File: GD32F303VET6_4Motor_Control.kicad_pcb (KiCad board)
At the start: 6 copper layers, 100 x 60 mm, 119 parts, among them CN1 KF128L-5.08-2P, CN2 WJ15EDGRC-3.81-2P, CN4 WJ15EDGRC-3.81-2P, CN5 KF2EDGRM-3.81-6P, CN6 KF2EDGRM-3.81-6P, CN7 KF2EDGRM-3.81-6P, CN8 KF2EDGRM-3.81-6P, J1 TYPE-C-31-M-31, J2 TYPE-C 16PIN 2MD(073), Q3 CJ3134K KF, Q4 CJ3134K KF, SW1 SKRPACE010, U1 XL1509-5.0, U10 SIT3485ESA, U11 TXS0104EPWR, U13 CH340E, U14 TPD4S012DRYR, U2 B0503S-2WR3L, U3 SY8089A1AAC, U4 CH213K, U5 SY8089AAC, U6 GD32F303VET6, U7 ISO1050DWR, U9 π131U30, Y1 TAXM8M4RDBCCT2T, Y2 XKXGI-SUA-32.768K

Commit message: 更新六层电机控制板设计与器件库
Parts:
- removed U2: B0503S-2WR3L, Converter_DCDC:B0503S-2WR3L
- added U15: IB0505S-2W3L, kicad_api_lib:IB0505S-2W3L, F.Cu at (165.4, 94.0)
- C13, C15, C36: footprint Capacitor_SMD:C_0402_1005Metric_Pad0.74x0.62mm_HandSolder -> Capacitor_SMD:C_0603_1608Metric_Pad1.08x0.95mm_HandSolder
- C4: value 10uF -> 4.7uF
- L1: value 1uF -> MWTC201610S1R0MT; footprint Capacitor_SMD:C_0603_1608Metric_Pad1.08x0.95mm_HandSolder -> kicad_api_lib:MWTC201610S1R0MT
- R5: footprint Resistor_SMD:R_0402_1005Metric_Pad0.72x0.64mm_HandSolder -> Resistor_SMD:R_0603_1608Metric_Pad0.98x0.95mm_HandSolder
- R8, R9: footprint Resistor_SMD:R_01005_0402Metric_Pad0.57x0.30mm_HandSolder -> Resistor_SMD:R_0603_1608Metric_Pad0.98x0.95mm_HandSolder
- U7: footprint Package_SO:SOIC-16_3.9x9.9mm_P1.27mm -> Package_SO:SOIC-16W_7.5x10.3mm_P1.27mm
- moved R5 12.6 mm to (152.9, 96.8)
- moved R1 7.61 mm to (140.7, 108.2), turned to 180 degrees
- moved C15 7.42 mm to (146.7, 108.1), turned to 0 degrees
- moved D2 6.55 mm to (143.6, 107.3), turned to 90 degrees
- moved C14 5.74 mm to (146.7, 106.4), turned to 0 degrees
- moved C13 5.04 mm to (147.8, 97.6), turned to 90 degrees
- moved C10 4.87 mm to (151.0, 106.9), turned to 0 degrees
- moved C9 4.60 mm to (153.0, 104.4), turned to 180 degrees
- moved U5 3.80 mm to (151.5, 101.2)
- moved R8 3.22 mm to (149.4, 97.6), turned to 90 degrees
- moved R9 2.34 mm to (152.9, 98.4)
- moved L3 2.15 mm to (147.1, 103.1), turned to -90 degrees
- moved C5 1.65 mm to (160.4, 99.5)
- moved L1 1.35 mm to (160.8, 81.1), turned to -90 degrees
- moved U7 1.03 mm to (99.0, 101.5)
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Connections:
- C44 pad 2: +5V_ISO -> +3V3_ISO
- R1 pad 2: GNDS -> GND
- R27 pad 2: /MCU_Core/USB_TTL_CH340/CH_TX -> /MCU_Core/USB_TTL_CH340/CH_RX
- U13 pad 8: /MCU_Core/USB_TTL_CH340/CH_RX -> /MCU_Core/USB_TTL_CH340/CH_TX
- U13 pad 9: /MCU_Core/USB_TTL_CH340/CH_TX -> /MCU_Core/USB_TTL_CH340/CH_RX
- U6 pad 23: (no net) -> /MCU_Core/FG1_4
- U6 pad 96: /MCU_Core/FG1_4 -> (no net)
- U9 pad 12: /MCU_Core/RS485_TX -> /RS485/RS485_RX
- U9 pad 16: +5V_ISO -> +3V3_ISO
- U9 pad 3: /MCU_Core/RS485_RX -> /MCU_Core/RS485_TX
- U9 pad 5: /RS485/RS485_RX -> /MCU_Core/RS485_RX
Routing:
- net +5V_ISO: track 74.6 -> 17.4 mm, vias 3 -> 2
- net GND: track 206.1 -> 184.7 mm, vias 102 -> 148
- net /MCU_Core/FG1_4: track 40.6 -> 60.3 mm
- net GNDS: track 75.5 -> 63.8 mm, vias 33 -> 32
- net Net-(U5-EN): track 8.65 -> 19.2 mm
- net /MCU_Core/RS485_TX: track 56.3 -> 47.6 mm
- net +5V: track 94.2 -> 87.6 mm, vias 7 -> 31
- net Net-(U5-FB): track 5.14 -> 10.7 mm
- net +3V3_ISO: track 24.5 -> 29.8 mm, vias 2 -> 3
- net /MCU_Core/RS485_RX: track 47.8 -> 43.2 mm
- net /MCU_Core/DIR1_4: track 39.2 -> 43.2 mm
- net /MCU_Core/USB_TTL_CH340/CH_TX: track 21.6 -> 18.1 mm
- net /MCU_Core/CAN_RX: track 32.8 -> 36.1 mm
- net Net-(U3-LX): track 7.52 -> 5.11 mm
- net +3V3: track 121.6 -> 123.9 mm, vias 14 -> 26
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- added copper zone on F.Cu, net +3V3
- added copper zone on F.Cu, net +5V

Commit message: 更新电源与USB供电设计、PCB及器件库
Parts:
- removed the R27 at (108.0, 73.0)
- removed R35: 5.1K, Resistor_SMD:R_0402_1005Metric_Pad0.72x0.64mm_HandSolder
- removed U15: IB0505S-2W3L, kicad_api_lib:IB0505S-2W3L
- added C55: 1uF/10V, Capacitor_SMD:C_0603_1608Metric, B.Cu at (88.9, 74.5)
- added C56: 1uF/10V, Capacitor_SMD:C_0603_1608Metric, B.Cu at (88.8, 90.5)
- added C57: 4.7uF/10V, Capacitor_SMD:C_0603_1608Metric, F.Cu at (169.8, 93.3)
- added C58: 1uF/10V, Capacitor_SMD:C_0603_1608Metric, F.Cu at (173.5, 105.6)
- added R34: 5.1K, Resistor_SMD:R_0402_1005Metric_Pad0.72x0.64mm_HandSolder, F.Cu at (96.6, 91.8)
- added U16: LM66100DCKR, kicad_api_lib:LM66100DCKR, B.Cu at (90.8, 74.6)
- added U17: LM66100DCKR, kicad_api_lib:LM66100DCKR, B.Cu at (90.8, 90.4)
- added U18: LM66100DCKR, kicad_api_lib:LM66100DCKR, F.Cu at (173.2, 102.7)
- added U2: IB0505S-2W3L, kicad_api_lib:IB0505S-2W3L, F.Cu at (165.5, 94.0)
- C1: footprint Capacitor_SMD:CP_Elec_10x10.5 -> Capacitor_SMD:CP_Elec_8x10
- C5: footprint Capacitor_SMD:CP_Elec_5x5.4 -> Capacitor_SMD:CP_Elec_6.3x7.7
- C53: value 10uF -> 4.7uF
- moved D10 1.09 mm to (99.5, 86.3)
- moved D4 0.70 mm to (169.2, 99.7)
- moved R32 0.35 mm to (100.1, 89.1)
- moved L3 0.28 mm to (147.1, 102.8)
- moved D1 0.21 mm to (177.8, 108.7), turned to 180 degrees
- moved C13 0.20 mm to (147.6, 97.6)
- moved R8 0.20 mm to (149.2, 97.6)
- moved R31 0.15 mm to (100.1, 90.1)
- turned C16 to 0 degrees
- turned C21 to 180 degrees
- renumbered C4 to C3, C3 to C4, R28 to R27, R29 to R28, R30 to R29, R31 to R30, R32 to R31, R33 to R32, R34 to R33
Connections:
- C1 pad 1: Net-(D1-K) -> +24V
- C16 pad 2: Net-(C16-Pad2) -> /MCU_Core/OSCIN
- C21 pad 2: Net-(C21-Pad2) -> /MCU_Core/OSCOUT
- C5 pad 1: +5V -> BOARD_5V_RAW
- C53 pad 1: +5V -> USB1_VBUS
- C54 pad 1: +5V -> USB1_VBUS
- D1 pad 1: Net-(D1-K) -> +24V
- D1 pad 2: +24V -> GND
- J1 pad A4: +5V -> USB1_VBUS
- J1 pad A9: +5V -> USB1_VBUS
- J1 pad B4: +5V -> USB1_VBUS
- J1 pad B9: +5V -> USB1_VBUS
- J2 pad A4: +5V -> USB2_VBUS
- J2 pad A9: +5V -> USB2_VBUS
- J2 pad B4: +5V -> USB2_VBUS
- J2 pad B9: +5V -> USB2_VBUS
- L2 pad 2: +5V -> BOARD_5V_RAW
- U1 pad 1: Net-(D1-K) -> +24V
- U1 pad 3: +5V -> BOARD_5V_RAW
- U14 pad 6: +5V -> USB1_VBUS
- Y1 pad 2: Net-(C16-Pad2) -> GND
- Y1 pad 4: Net-(C21-Pad2) -> GND
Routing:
- net GND: track 184.7 -> 221.5 mm, vias 148 -> 155
- net Net-(D1-K): track 35.1 -> 0.00 mm
- net +24V: track 6.75 -> 38.2 mm
- net USB1_VBUS: track 0.00 -> 21.3 mm, vias 0 -> 2
- net USB2_VBUS: track 0.00 -> 11.2 mm, vias 0 -> 1
- net BOARD_5V_RAW: track 0.00 -> 7.25 mm, vias 0 -> 22
- net +5V: track 87.6 -> 93.2 mm, vias 31 -> 7
- net /MCU_Core/OSCOUT: track 12.4 -> 15.0 mm
- net Net-(C21-Pad2): track 2.16 -> 0.00 mm
- net /MCU_Core/USB_TTL_CH340/DP2: track 10.2 -> 12.3 mm
- net Net-(C16-Pad2): track 1.97 -> 0.00 mm
- net /MCU_Core/OSCIN: track 13.6 -> 15.5 mm
- net /MCU_Core/USB_TTL_CH340/DN2: track 11.7 -> 10.6 mm
- net /MCU_Core/USB_DP: track 21.8 -> 22.7 mm
- net Net-(U5-EN): track 19.2 -> 20.1 mm
- added copper zone on F.Cu, net BOARD_5V_RAW
- added copper zone on In2.Cu, net BOARD_5V_RAW
- removed copper zone on B.Cu, net GND

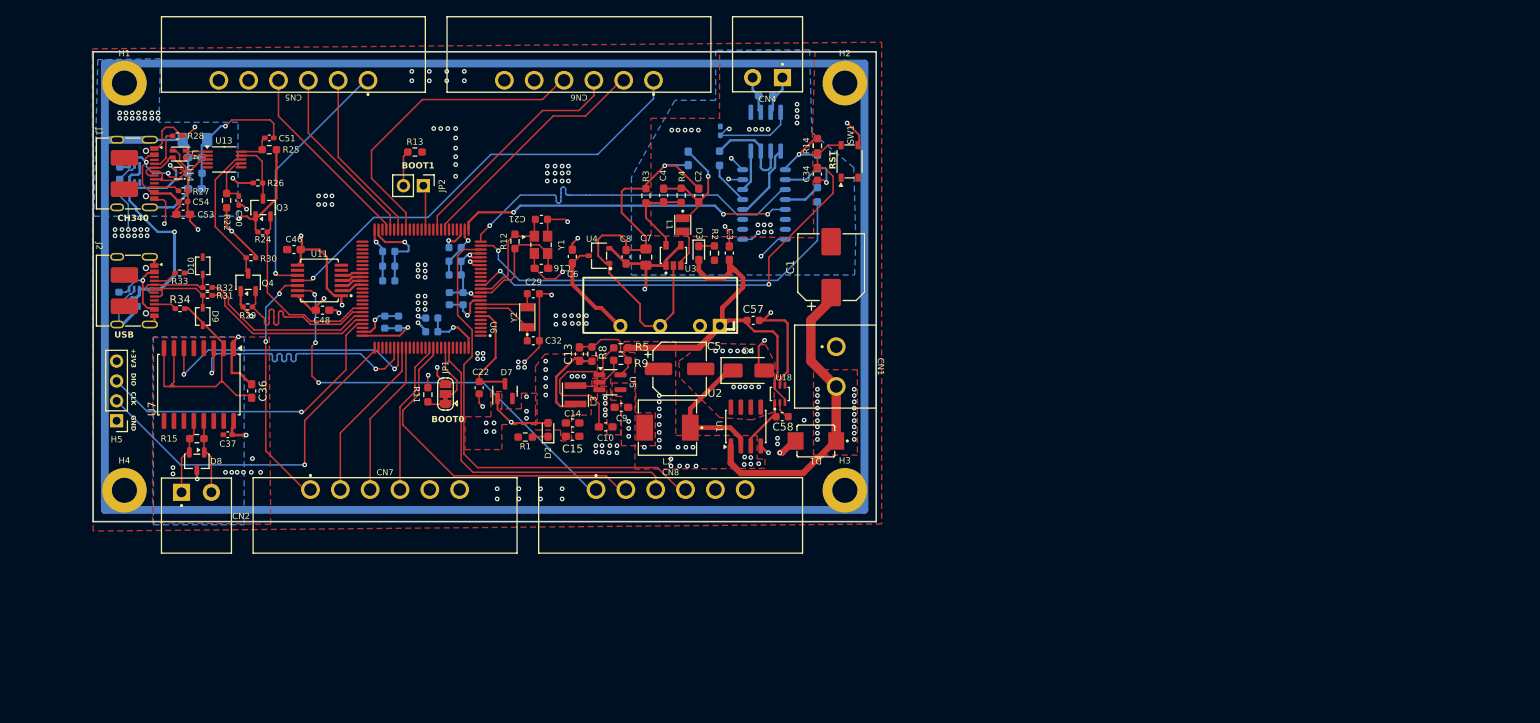
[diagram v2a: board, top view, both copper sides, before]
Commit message: V2.0: sync KiCad design, add firmware snapshot and README
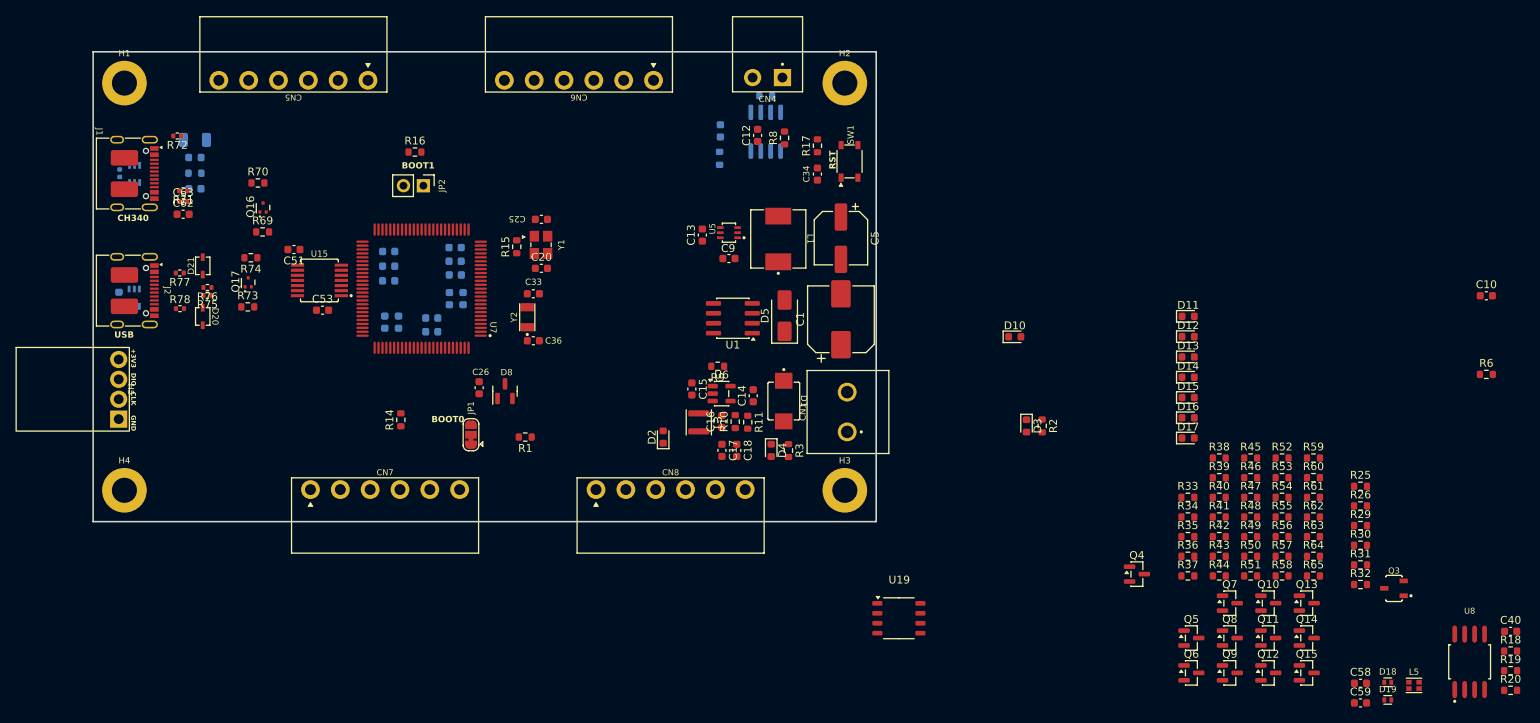
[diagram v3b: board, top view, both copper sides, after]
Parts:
- removed C2, C6: 10uF, Capacitor_SMD:C_0603_1608Metric_Pad1.08x0.95mm_HandSolder
- removed C3: 4.7uF, Capacitor_SMD:C_0603_1608Metric_Pad1.08x0.95mm_HandSolder
- removed the C36 at (105.8, 102.3)
- removed C37: 100nF, Capacitor_SMD:C_0402_1005Metric_Pad0.74x0.62mm_HandSolder
- removed C4: 22pF, Capacitor_SMD:C_0603_1608Metric_Pad1.08x0.95mm_HandSolder
- removed C43, C44: 0.1uF, Capacitor_SMD:C_0603_1608Metric_Pad1.08x0.95mm_HandSolder
- removed the C50 at (104.1, 78.0)
- removed the C51 at (108.0, 70.0)
- removed C7: 10uF, Capacitor_SMD:C_0805_2012Metric_Pad1.18x1.45mm_HandSolder
- removed C8: 1uF, Capacitor_SMD:C_0603_1608Metric_Pad1.08x0.95mm_HandSolder
- removed CN2: WJ15EDGRC-3.81-2P, kicad_api_lib:WJ15EDGRC-3.81-2P
- removed the D8 at (98.8, 111.3)
- removed the L1 at (160.8, 81.1)
- removed L4: PCAQ2012B-900T040, Inductor_SMD:L_CommonModeChoke_Coilcraft_0805USB
- removed the R15 at (98.8, 108.4)
- removed R22: 0, Resistor_SMD:R_0603_1608Metric_Pad0.98x0.95mm_HandSolder
- removed R4: 100k, Resistor_SMD:R_0603_1608Metric_Pad0.98x0.95mm_HandSolder
- removed the U13 at (102.2, 72.8)
- removed U14: TPD4S012DRYR, Package_DFN_QFN:TPD4S012DRYR
- removed U2: IB0505S-2W3L, kicad_api_lib:IB0505S-2W3L
- removed U3: SY8089A1AAC, kicad_api_lib:SY8089A1AAC
- removed U4: CH213K, kicad_api_lib:CH213K
- removed the U7 at (99.0, 101.5)
- removed U9: π131U30, kicad_api_lib:π131U30
- added C10: 1nF, Capacitor_SMD:C_0603_1608Metric, F.Cu at (263.4, 90.2)
- added C12: 1nF, Capacitor_SMD:C_0603_1608Metric, F.Cu at (170.4, 69.7)
- added C40: 100nF, Capacitor_SMD:C_0603_1608Metric, F.Cu at (266.5, 133.0)
- added C58: 1uF, Capacitor_SMD:C_0603_1608Metric, F.Cu at (247.4, 139.6)
- added C59: 100nF, Capacitor_SMD:C_0603_1608Metric, F.Cu at (247.4, 142.2)
- added D10: DIR_CMD_GREEN, LED_SMD:LED_0603_1608Metric, F.Cu at (203.2, 95.4)
- added D11: RELEASE_YELLOW, LED_SMD:LED_0603_1608Metric, F.Cu at (225.3, 92.8)
- added D12: DIR_CMD_GREEN, LED_SMD:LED_0603_1608Metric, F.Cu at (225.3, 95.4)
- added D13: RELEASE_YELLOW, LED_SMD:LED_0603_1608Metric, F.Cu at (225.3, 98.0)
- added D14: DIR_CMD_GREEN, LED_SMD:LED_0603_1608Metric, F.Cu at (225.3, 100.6)
- added D15: RELEASE_YELLOW, LED_SMD:LED_0603_1608Metric, F.Cu at (225.3, 103.1)
- added D16: DIR_CMD_GREEN, LED_SMD:LED_0603_1608Metric, F.Cu at (225.3, 105.7)
- added D17: RELEASE_YELLOW, LED_SMD:LED_0603_1608Metric, F.Cu at (225.3, 108.3)
- added D18: KLXES15AAA1, kicad_api_lib:KLXES15AAA1, F.Cu at (250.8, 139.5)
- added D19: KLXES15AAA1, kicad_api_lib:KLXES15AAA1, F.Cu at (250.8, 141.8)
- added D4: LED, LED_SMD:LED_0603_1608Metric, F.Cu at (172.1, 109.9)
- added L5: PCAQ2012B-900T040, kicad_api_lib:PCAQ2012B-900T040, F.Cu at (254.2, 139.9)
- added Q10: CJ3134K, Package_TO_SOT_SMD:SOT-23, F.Cu at (235.6, 129.4)
- added Q11: CJ3134K, Package_TO_SOT_SMD:SOT-23, F.Cu at (235.6, 133.9)
- added Q12: CJ3134K, Package_TO_SOT_SMD:SOT-23, F.Cu at (235.6, 138.3)
- added Q13: CJ3134K, Package_TO_SOT_SMD:SOT-23, F.Cu at (240.5, 129.4)
- added Q14: CJ3134K, Package_TO_SOT_SMD:SOT-23, F.Cu at (240.5, 133.9)
- added Q15: CJ3134K, Package_TO_SOT_SMD:SOT-23, F.Cu at (240.5, 138.3)
- added Q3: CJ3134K, kicad_api_lib:CJ3134K, F.Cu at (251.6, 127.5)
- added Q4: CJ3134K, Package_TO_SOT_SMD:SOT-23, F.Cu at (218.8, 125.7)
- added Q5: CJ3134K, Package_TO_SOT_SMD:SOT-23, F.Cu at (225.8, 133.9)
- added Q6: CJ3134K, Package_TO_SOT_SMD:SOT-23, F.Cu at (225.8, 138.3)
- added Q7: CJ3134K, Package_TO_SOT_SMD:SOT-23, F.Cu at (230.7, 129.4)
- added Q8: CJ3134K, Package_TO_SOT_SMD:SOT-23, F.Cu at (230.7, 133.9)
- added Q9: CJ3134K, Package_TO_SOT_SMD:SOT-23, F.Cu at (230.7, 138.3)
- added R19: 10kΩ, Resistor_SMD:R_0603_1608Metric, F.Cu at (266.5, 138.0)
- added R20: 10kΩ, Resistor_SMD:R_0603_1608Metric, F.Cu at (266.5, 140.5)
- added R26: 360, Resistor_SMD:R_0603_1608Metric, F.Cu at (247.4, 117.0)
- added R29: AF0603JR-0710KL, Resistor_SMD:R_0603_1608Metric, F.Cu at (247.4, 119.5)
- added R30: AF0603JR-0710KL, Resistor_SMD:R_0603_1608Metric, F.Cu at (247.4, 122.0)
- added R31: 330, Resistor_SMD:R_0603_1608Metric, F.Cu at (247.4, 124.5)
- added R32: 4.7k, Resistor_SMD:R_0603_1608Metric, F.Cu at (247.4, 127.0)
- added R33: 100, Resistor_SMD:R_0603_1608Metric, F.Cu at (225.3, 115.9)
- added R34: 1k, Resistor_SMD:R_0603_1608Metric, F.Cu at (225.3, 118.4)
- added R35: 1k, Resistor_SMD:R_0603_1608Metric, F.Cu at (225.3, 120.9)
- added R36: 100, Resistor_SMD:R_0603_1608Metric, F.Cu at (225.3, 123.4)
- added R37: 1k, Resistor_SMD:R_0603_1608Metric, F.Cu at (225.3, 125.9)
- added R38: 1k, Resistor_SMD:R_0603_1608Metric, F.Cu at (229.3, 110.9)
- added R39: 10k, Resistor_SMD:R_0603_1608Metric, F.Cu at (229.3, 113.4)
- added R40: 10k, Resistor_SMD:R_0603_1608Metric, F.Cu at (229.3, 115.9)
- added R41: 10kΩ, Resistor_SMD:R_0603_1608Metric, F.Cu at (229.3, 118.4)
- added R42: 100, Resistor_SMD:R_0603_1608Metric, F.Cu at (229.3, 120.9)
- added R43: 100, Resistor_SMD:R_0603_1608Metric, F.Cu at (229.3, 123.4)
- added R44: 10k, Resistor_SMD:R_0603_1608Metric, F.Cu at (229.3, 125.9)
- added R45: 10k, Resistor_SMD:R_0603_1608Metric, F.Cu at (233.3, 110.9)
- added R46: 4.7kΩ, Resistor_SMD:R_0603_1608Metric, F.Cu at (233.3, 113.4)
- added R47: 4.7kΩ, Resistor_SMD:R_0603_1608Metric, F.Cu at (233.3, 115.9)
- added R48: 10k, Resistor_SMD:R_0603_1608Metric, F.Cu at (233.3, 118.4)
- added R49: 10k, Resistor_SMD:R_0603_1608Metric, F.Cu at (233.3, 120.9)
- added R50: 4.7kΩ, Resistor_SMD:R_0603_1608Metric, F.Cu at (233.3, 123.4)
- added R51: 4.7kΩ, Resistor_SMD:R_0603_1608Metric, F.Cu at (233.3, 125.9)
- added R52: 100, Resistor_SMD:R_0603_1608Metric, F.Cu at (237.3, 110.9)
- added R53: 1k, Resistor_SMD:R_0603_1608Metric, F.Cu at (237.3, 113.4)
- added R54: 1k, Resistor_SMD:R_0603_1608Metric, F.Cu at (237.3, 115.9)
- added R55: 100, Resistor_SMD:R_0603_1608Metric, F.Cu at (237.3, 118.4)
- added R56: 1k, Resistor_SMD:R_0603_1608Metric, F.Cu at (237.3, 120.9)
- added R57: 1k, Resistor_SMD:R_0603_1608Metric, F.Cu at (237.3, 123.4)
- added R58: 10k, Resistor_SMD:R_0603_1608Metric, F.Cu at (237.3, 125.9)
- added R59: 10k, Resistor_SMD:R_0603_1608Metric, F.Cu at (241.3, 110.9)
- added R6: 1MΩ, Resistor_SMD:R_0603_1608Metric, F.Cu at (263.4, 100.2)
- added R60: 100, Resistor_SMD:R_0603_1608Metric, F.Cu at (241.3, 113.4)
- added R61: 100, Resistor_SMD:R_0603_1608Metric, F.Cu at (241.3, 115.9)
- added R62: 10k, Resistor_SMD:R_0603_1608Metric, F.Cu at (241.3, 118.4)
- added R63: 10k, Resistor_SMD:R_0603_1608Metric, F.Cu at (241.3, 120.9)
- added R64: 10k, Resistor_SMD:R_0603_1608Metric, F.Cu at (241.3, 123.4)
- added R65: 10k, Resistor_SMD:R_0603_1608Metric, F.Cu at (241.3, 125.9)
- added R8: 1MΩ, Resistor_SMD:R_0603_1608Metric, F.Cu at (173.8, 70.0)
- added U19: CH340N, kicad_api_lib:CH340N, F.Cu at (188.4, 131.3)
- added U8: GD25Q16ESIGR, kicad_api_lib:GD25Q16ESIGR, F.Cu at (261.3, 136.9)
- C1: value 470µF -> RVT1E471M0810; footprint Capacitor_SMD:CP_Elec_8x10 -> kicad_api_lib:RVT1E471M0810
- C11: footprint Capacitor_SMD:C_0603_1608Metric_Pad1.08x0.95mm_HandSolder -> Capacitor_SMD:C_0603_1608Metric
- C13: renamed from C57; value 4.7uF/10V -> 1uF/10V
- C14: renamed from C9; value 10uF -> 22uF; footprint Capacitor_SMD:C_0603_1608Metric_Pad1.08x0.95mm_HandSolder -> Capacitor_SMD:C_0603_1608Metric
- C15: renamed from C10; footprint Capacitor_SMD:C_0603_1608Metric_Pad1.08x0.95mm_HandSolder -> Capacitor_SMD:C_0603_1608Metric
- C16: renamed from C13; value 100nF -> 22pF; footprint Capacitor_SMD:C_0603_1608Metric_Pad1.08x0.95mm_HandSolder -> Capacitor_SMD:C_0603_1608Metric
- C17: renamed from C14; footprint Capacitor_SMD:C_0603_1608Metric_Pad1.08x0.95mm_HandSolder -> Capacitor_SMD:C_0603_1608Metric
- C18: renamed from C15; footprint Capacitor_SMD:C_0603_1608Metric_Pad1.08x0.95mm_HandSolder -> Capacitor_SMD:C_0603_1608Metric
- C20: renamed from C16; value 22pF -> 15pF; footprint Capacitor_SMD:C_0603_1608Metric_Pad1.08x0.95mm_HandSolder -> Capacitor_SMD:C_0603_1608Metric
- C25: renamed from C21; value 22pF -> 15pF
- C33: renamed from C29; value 12pF -> 15pF
- C36: renamed from C32; value 12pF -> 15pF
- C5: value 220µF -> RVT1E221M0607; footprint Capacitor_SMD:CP_Elec_6.3x7.7 -> kicad_api_lib:RVT1E221M0607
- C50: renamed from C45; footprint Capacitor_SMD:C_0402_1005Metric_Pad0.74x0.62mm_HandSolder -> Capacitor_SMD:C_0603_1608Metric
- C51: renamed from C46; value 0.1uF -> 100nF; footprint Capacitor_SMD:C_0603_1608Metric_Pad1.08x0.95mm_HandSolder -> Capacitor_SMD:C_0603_1608Metric
- C53: renamed from C48; value 0.1uF -> 100nF; footprint Capacitor_SMD:C_0603_1608Metric_Pad1.08x0.95mm_HandSolder -> Capacitor_SMD:C_0603_1608Metric
- C57: renamed from C55; footprint Capacitor_SMD:C_0603_1608Metric -> Capacitor_SMD:C_0402_1005Metric
- C60: renamed from C52; value 1nF -> CC1206MKX7RDBB102; footprint Capacitor_SMD:C_1206_3216Metric_Pad1.33x1.80mm_HandSolder -> kicad_api_lib:CC1206MKX7RDBB102
- C62: renamed from C53; value 4.7uF -> 0603X106M100NT; footprint Capacitor_SMD:C_0603_1608Metric_Pad1.08x0.95mm_HandSolder -> Capacitor_SMD:C_0603_1608Metric
- C63: renamed from C54; value 100nF -> C1005X5R1H104K050BB; footprint Capacitor_SMD:C_0402_1005Metric_Pad0.74x0.62mm_HandSolder -> Capacitor_SMD:C_0402_1005Metric
- CN5, CN6, CN7, CN8: value KF2EDGRM-3.81-6P -> KF15EDGRC3.81-6P; footprint kicad_api_lib:KF2EDGRM-3.81-6P -> kicad_api_lib:KF15EDGRC3.81-6P
- D2, D3: footprint LED_SMD:LED_0603_1608Metric_Pad1.05x0.95mm_HandSolder -> LED_SMD:LED_0603_1608Metric
- FB2: value 100ohm@100MHz -> UPZ1608E101-3R0TF; footprint Capacitor_SMD:C_0603_1608Metric_Pad1.08x0.95mm_HandSolder -> kicad_api_lib:UPZ1608E101-3R0TF
- H5: footprint Connector_PinHeader_2.54mm:PinHeader_1x04_P2.54mm_Vertical -> kicad_api_lib:X9254WR-04-N0SN
- J1, J2: footprint kicad_api_lib:TYPE-C 16PIN 2MD NEW(073) -> kicad_api_lib:TYPE-C-31-M-31
- L3: footprint Inductor_SMD_Wurth:L_Wurth_WE-LQSH-3012 -> kicad_api_lib:SWPA3015S2R2NT
- Q16: renamed from Q3; footprint Package_TO_SOT_SMD:SOT-23-3 -> kicad_api_lib:CJ3134K KF
- Q17: renamed from Q4; footprint Package_TO_SOT_SMD:SOT-23-3 -> kicad_api_lib:CJ3134K KF
- R1, R2: value 10k -> 10kΩ; footprint Resistor_SMD:R_0603_1608Metric_Pad0.98x0.95mm_HandSolder -> Resistor_SMD:R_0603_1608Metric
- R10: renamed from R8; value 100K -> 100k; footprint Resistor_SMD:R_0603_1608Metric_Pad0.98x0.95mm_HandSolder -> Resistor_SMD:R_0603_1608Metric
- R11: renamed from R9; value 22K -> 22.1k; footprint Resistor_SMD:R_0603_1608Metric_Pad0.98x0.95mm_HandSolder -> Resistor_SMD:R_0603_1608Metric
- R14: renamed from R11; footprint Resistor_SMD:R_0603_1608Metric_Pad0.98x0.95mm_HandSolder -> Resistor_SMD:R_0603_1608Metric
- R15: renamed from R12; footprint Resistor_SMD:R_0603_1608Metric_Pad0.98x0.95mm_HandSolder -> Resistor_SMD:R_0603_1608Metric
- R16: renamed from R13; footprint Resistor_SMD:R_0603_1608Metric_Pad0.98x0.95mm_HandSolder -> Resistor_SMD:R_0603_1608Metric
- R17: renamed from R14; footprint Resistor_SMD:R_0603_1608Metric_Pad0.98x0.95mm_HandSolder -> Resistor_SMD:R_0603_1608Metric
- R18: value 10K -> 10kΩ; footprint Resistor_SMD:R_0603_1608Metric_Pad0.98x0.95mm_HandSolder -> Resistor_SMD:R_0603_1608Metric; moved to F.Cu
- R25: value 0 -> 360; footprint Resistor_SMD:R_0603_1608Metric_Pad0.98x0.95mm_HandSolder -> Resistor_SMD:R_0603_1608Metric
- R27: renamed from R19; value 120 -> CRCW0603120RFKEA; footprint Resistor_SMD:R_0603_1608Metric_Pad0.98x0.95mm_HandSolder -> Resistor_SMD:R_0603_1608Metric
- R28: renamed from R20; value 10K -> 1k; footprint Resistor_SMD:R_0603_1608Metric_Pad0.98x0.95mm_HandSolder -> Resistor_SMD:R_0603_1608Metric
- R3: value 22.1k -> 10kΩ; footprint Resistor_SMD:R_0603_1608Metric_Pad0.98x0.95mm_HandSolder -> Resistor_SMD:R_0603_1608Metric
- R69: renamed from R24; value 4.7K -> 4.7k; footprint Resistor_SMD:R_0402_1005Metric_Pad0.72x0.64mm_HandSolder -> Resistor_SMD:R_0603_1608Metric
- R7: renamed from R6; value 1M -> 1MΩ; footprint Resistor_SMD:R_0603_1608Metric_Pad0.98x0.95mm_HandSolder -> Resistor_SMD:R_0603_1608Metric
- R70: renamed from R26; value 4.7K -> 4.7k; footprint Resistor_SMD:R_0402_1005Metric_Pad0.72x0.64mm_HandSolder -> Resistor_SMD:R_0603_1608Metric
- R71: renamed from R27; value 5.1K -> RC0402FR-075K1L; footprint Resistor_SMD:R_0402_1005Metric_Pad0.72x0.64mm_HandSolder -> Resistor_SMD:R_0402_1005Metric
- R72: renamed from R28; value 5.1K -> RC0402FR-075K1L; footprint Resistor_SMD:R_0402_1005Metric_Pad0.72x0.64mm_HandSolder -> Resistor_SMD:R_0402_1005Metric
- R73: renamed from R29; value 4.7K -> 4.7k; footprint Resistor_SMD:R_0402_1005Metric_Pad0.72x0.64mm_HandSolder -> Resistor_SMD:R_0603_1608Metric
- R74: renamed from R30; value 4.7K -> 4.7k; footprint Resistor_SMD:R_0402_1005Metric_Pad0.72x0.64mm_HandSolder -> Resistor_SMD:R_0603_1608Metric
- R75: renamed from R31; value 22 -> 0402WGF220JTCE; footprint Resistor_SMD:R_0402_1005Metric_Pad0.72x0.64mm_HandSolder -> Resistor_SMD:R_0402_1005Metric
- R76: renamed from R32; value 22 -> 0402WGF220JTCE; footprint Resistor_SMD:R_0402_1005Metric_Pad0.72x0.64mm_HandSolder -> Resistor_SMD:R_0402_1005Metric
- R77: renamed from R33; value 5.1K -> 0402WGF5101TCE; footprint Resistor_SMD:R_0402_1005Metric_Pad0.72x0.64mm_HandSolder -> Resistor_SMD:R_0402_1005Metric
- R78: renamed from R34; value 5.1K -> 0402WGF5101TCE; footprint Resistor_SMD:R_0402_1005Metric_Pad0.72x0.64mm_HandSolder -> Resistor_SMD:R_0402_1005Metric
- R9: renamed from R5; value 10K -> 10k; footprint Resistor_SMD:R_0603_1608Metric_Pad0.98x0.95mm_HandSolder -> Resistor_SMD:R_0603_1608Metric
- U1: footprint Package_SO:SOIC-8_3.9x4.9mm_P1.27mm -> kicad_api_lib:XL1509-5.0
- U13: renamed from U10; footprint Package_SO:SOIC-8_3.9x4.9mm_P1.27mm -> kicad_api_lib:SIT3485ESA
- U6: renamed from U5; value SY8089AAC -> SY8089A1AAC; footprint Package_TO_SOT_SMD:SOT-23-5_HandSoldering -> Package_TO_SOT_SMD:SOT-23-5
- moved R25 145.8 mm to (247.4, 114.5), turned to 0 degrees
- moved R18 106.0 mm to (266.5, 135.5), turned to 0 degrees
- moved D3 47.3 mm to (204.7, 106.8)
- moved R2 47.3 mm to (206.7, 106.8)
- moved R3 37.3 mm to (174.3, 109.9)
- moved L1 27.9 mm to (173.0, 82.9), turned to 90 degrees
- moved C5 26.5 mm to (181.0, 82.8), turned to -90 degrees
- moved U5 21.6 mm to (166.7, 82.1), turned to 90 degrees
- moved C9 21.3 mm to (166.7, 85.4), turned to 180 degrees
- moved C18 21.0 mm to (167.7, 109.9), turned to -90 degrees
- moved R10 20.2 mm to (167.5, 106.2)
- moved C16 20.1 mm to (165.8, 106.2)
- moved C17 19.4 mm to (165.8, 109.9), turned to -90 degrees
- moved R11 18.0 mm to (169.1, 106.3), turned to -90 degrees
- moved C14 16.9 mm to (169.8, 102.9), turned to 90 degrees
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- renumbered C17 to C21, C18 to C22, C19 to C23, C20 to C24, C22 to C26, C23 to C27, C24 to C28, C25 to C29, C26 to C30, C27 to C31, C28 to C32, C30 to C34, C31 to C35, C35 to C39, C56 to C61, C58 to C9, D9 to D20, D10 to D21, D4 to D5, D7 to D8, L2 to L1, U11 to U15, U16 to U20, U17 to U21, U18 to U5, U6 to U7
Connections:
- net VBAT renamed VCC
- C50 pad 1: +3V3_ISO -> +3V3
- C50 pad 2: GNDS -> GND
- CN5 pad 2: /MCU_Core/BRAKE1_1 -> /MCU_Core/Motor_Comm/MOTOR_BRAKE1_1
- CN5 pad 3: /MCU_Core/DIR1_1 -> /MCU_Core/Motor_Comm/MOTOR_DIR1_1
- CN6 pad 2: /MCU_Core/BRAKE1_2 -> /MCU_Core/Motor_Comm/MOTOR_BRAKE1_2
- CN6 pad 3: /MCU_Core/DIR1_2 -> /MCU_Core/Motor_Comm/MOTOR_DIR1_2
- CN7 pad 2: /MCU_Core/BRAKE1_3 -> /MCU_Core/Motor_Comm/MOTOR_BRAKE1_3
- CN7 pad 3: /MCU_Core/DIR1_3 -> /MCU_Core/Motor_Comm/MOTOR_DIR1_3
- CN8 pad 2: /MCU_Core/BRAKE1_4 -> /MCU_Core/Motor_Comm/MOTOR_BRAKE1_4
- CN8 pad 3: /MCU_Core/DIR1_4 -> /MCU_Core/Motor_Comm/MOTOR_DIR1_4
- D2 pad 2: +3V3 -> +5V
- D20 pad 1: GND -> Earth
- D21 pad 2: GND -> Earth
- D3 pad 2: +5V -> +3V3
- H5 pad 4: +3V3 -> +5V
- J2 pad MH1: GND -> Earth
- J2 pad MH2: GND -> Earth
- J2 pad MH3: GND -> Earth
- J2 pad MH4: GND -> Earth
- R18 pad 1: Net-(U9-VIB) -> /MCU_Core/MCU_SPI_NSS
- R18 pad 2: /MCU_Core/RS485_DE -> +3V3
- R25 pad 2: Net-(U13-V3) -> /RS485/RS485A
- R28 pad 2: /RS485/CTRL -> Net-(Q3-D)
- R3 pad 1: GNDS -> +24V
- R3 pad 2: /POWER/FB1 -> Net-(D4-A)
- U13 pad 1: /RS485/RS485_RX -> /MCU_Core/RS485_RX
- U13 pad 4: /RS485/RS485_TX -> GND
- U13 pad 5: GNDS -> GND
- U13 pad 8: +3V3_ISO -> +3V3
- U15 pad 8: +3V3 -> /MCU_Core/Motor_start
- U7 pad 1: (no net) -> unconnected-(U7E-PE2/EXMC_A23-Pad1)
- U7 pad 2: (no net) -> unconnected-(U7E-PE3/EXMC_A19-Pad2)
- U7 pad 29: (no net) -> unconnected-(U7E-PA4/SPI0_NSS/USART1_CK/ADC01_IN4/DAC_OUT-Pad29)
- U7 pad 3: (no net) -> unconnected-(U7E-PE4/EXMC_A20-Pad3)
- U7 pad 30: (no net) -> unconnected-(U7E-PA5/SPI0_SCK/ADC01_IN5/DAC0_OUT1-Pad30)
- U7 pad 31: (no net) -> unconnected-(U7E-PA6/SPI0_MISO/ADC01_IN6/TIMER2_CH0/TIMER7_BRKIN-Pad31)
- U7 pad 33: (no net) -> unconnected-(U7E-PC4/ADC01_IN14-Pad33)
- U7 pad 35: (no net) -> unconnected-(U7E-PB0/ADC01_IN8/TIMER2_CH2/TIMER7_CH1_ON-Pad35)
- U7 pad 36: (no net) -> unconnected-(U7E-PB1/ADC01_IN9/TIMER2_CH3/TIMER7_CH2_ON-Pad36)
- U7 pad 38: (no net) -> unconnected-(U7E-PE7/EXMC_D4-Pad38)
- U7 pad 39: (no net) -> unconnected-(U7E-PE8/EXMC_D5-Pad39)
- U7 pad 4: (no net) -> unconnected-(U7E-PE5/EXMC_A21-Pad4)
- U7 pad 40: (no net) -> unconnected-(U7E-PE9/EXMC_D6-Pad40)
- U7 pad 41: (no net) -> unconnected-(U7E-PE10/EXMC_D7-Pad41)
- U7 pad 43: (no net) -> unconnected-(U7E-PE12/EXMC_D9-Pad43)
- U7 pad 45: (no net) -> unconnected-(U7E-PE14/EXMC_D11-Pad45)
- U7 pad 48: (no net) -> unconnected-(U7E-PB11/I2C1_SDA/USART2_RX-Pad48)
- U7 pad 5: (no net) -> unconnected-(U7E-PE6/EXMC_A22-Pad5)
- U7 pad 51: (no net) -> /MCU_Core/MCU_SPI_NSS
- U7 pad 52: (no net) -> /MCU_Core/MCU_SPI_SLK
- U7 pad 53: (no net) -> /MCU_Core/MCU_SPI_MISO
- U7 pad 54: (no net) -> /MCU_Core/MCU_SPI_MOSI
- U7 pad 55: (no net) -> unconnected-(U7E-PD8/EXMC_D13-Pad55)
- U7 pad 56: (no net) -> unconnected-(U7E-PD9/EXMC_D14-Pad56)
- U7 pad 57: (no net) -> unconnected-(U7E-PD10/EXMC_D15-Pad57)
- U7 pad 58: (no net) -> /MCU_Core/Motor_start
- U7 pad 63: (no net) -> unconnected-(U7E-PC6/I2S1_MCK/TIMER7_CH0/SDIO_D6-Pad63)
- U7 pad 64: (no net) -> unconnected-(U7E-PC7/I2S2_MCK/TIMER7_CH1/SDIO_D7-Pad64)
- U7 pad 65: (no net) -> unconnected-(U7E-PC8/TIMER7_CH2/SDIO_D0-Pad65)
- U7 pad 66: (no net) -> unconnected-(U7E-PC9/TIMER7_CH3/SDIO_D1-Pad66)
- U7 pad 67: (no net) -> unconnected-(U7E-PA8/USART0_CK/TIMER0_CH0/CK_OUT0/CTC_SYNC-Pad67)
- U7 pad 7: (no net) -> unconnected-(U7E-PC13/TAMPER-RTC-Pad7)
- U7 pad 73: (no net) -> unconnected-(U7E-NC-Pad73)
- U7 pad 77: (no net) -> unconnected-(U7E-PA15/JTDI/SPI2_NSS/I2S2_WS-Pad77)
- U7 pad 80: (no net) -> unconnected-(U7E-PC12/UART4_TX/SDIO_CK-Pad80)
- U7 pad 85: (no net) -> unconnected-(U7E-PD4/EXMC_NOE-Pad85)
- U7 pad 86: (no net) -> unconnected-(U7E-PD5/EXMC_NWE-Pad86)
- U7 pad 87: (no net) -> unconnected-(U7E-PD6/EXMC_NWAIT-Pad87)
- U7 pad 88: (no net) -> unconnected-(U7E-PD7/EXMC_NE0/EXMC_NCE1-Pad88)
- U7 pad 89: (no net) -> unconnected-(U7E-PB3/JTDO/SPI2_SCK/I2S2_CK-Pad89)
- U7 pad 92: (no net) -> unconnected-(U7E-PB6/I2C0_SCL/TIMER3_CH0-Pad92)
- U7 pad 93: (no net) -> unconnected-(U7E-PB7/I2C0_SDA/TIMER3_CH1/EXMC_NADV-Pad93)
- U7 pad 96: (no net) -> unconnected-(U7E-PB9/TIMER3_CH3/SDIO_D5-Pad96)
- U7 pad 97: (no net) -> unconnected-(U7E-PE0/TIMER3_ETI/EXMC_NBL0-Pad97)
- U7 pad 98: (no net) -> unconnected-(U7E-PE1/EXMC_NBL1-Pad98)
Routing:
- net Earth: track 340.7 -> 0.00 mm
- net GND: track 221.5 -> 0.00 mm, vias 155 -> 0
- net +3V3: track 123.9 -> 0.00 mm, vias 26 -> 0
- net +5V: track 93.2 -> 0.00 mm, vias 7 -> 0
- net GNDS: track 63.9 -> 0.00 mm, vias 32 -> 0
- net /MCU_Core/NRST: track 63.5 -> 0.00 mm, vias 2 -> 0
- net /MCU_Core/FG1_4: track 60.3 -> 0.00 mm
- net /MCU_Core/Motor_Comm/PWM1_5V_2: track 57.8 -> 0.00 mm, vias 1 -> 0
- net /MCU_Core/Motor_Comm/PWM1_5V_4: track 55.7 -> 0.00 mm, vias 3 -> 0
- net /MCU_Core/RS485_DE: track 52.5 -> 0.00 mm, vias 1 -> 0
- net /MCU_Core/RS485_TX: track 47.6 -> 0.00 mm, vias 1 -> 0
- net /MCU_Core/SWCLK: track 46.1 -> 0.00 mm, vias 1 -> 0
- net /MCU_Core/BRAKE1_4: track 43.7 -> 0.00 mm
- net /MCU_Core/RS485_RX: track 43.2 -> 0.00 mm, vias 3 -> 0
- net /MCU_Core/DIR1_4: track 43.2 -> 0.00 mm
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- removed copper zone on F.Cu, net +24V
- removed copper zone on In3.Cu, net +24V
- removed copper zone on F.Cu, net +3V3
- removed copper zone on In2.Cu, net +3V3
- removed copper zone on In2.Cu, net +3V3_ISO
- removed copper zone on F.Cu, net +5V
- removed copper zone on In2.Cu, net +5V
- removed copper zone on In2.Cu, net +5V_ISO
- removed copper zone on F.Cu, net BOARD_5V_RAW
- removed copper zone on In2.Cu, net BOARD_5V_RAW
- removed copper zone on B.Cu, net Earth
- removed copper zone on In1.Cu, net Earth
- removed copper zone on F.Cu, net GND
- removed copper zone on In4.Cu, net GND
- removed copper zone on B.Cu, net GNDS
- removed copper zone on F.Cu, net GNDS
- removed copper zone on In1.Cu, net GNDS
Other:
- board text removed: "CANH"
- board text removed: "CANL"
